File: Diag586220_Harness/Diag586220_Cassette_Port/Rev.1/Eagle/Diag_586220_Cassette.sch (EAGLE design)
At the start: 11 parts, among them J1 C64-TAPEPORT, J4 C64-TAPEPORTM, Q1 BC547B

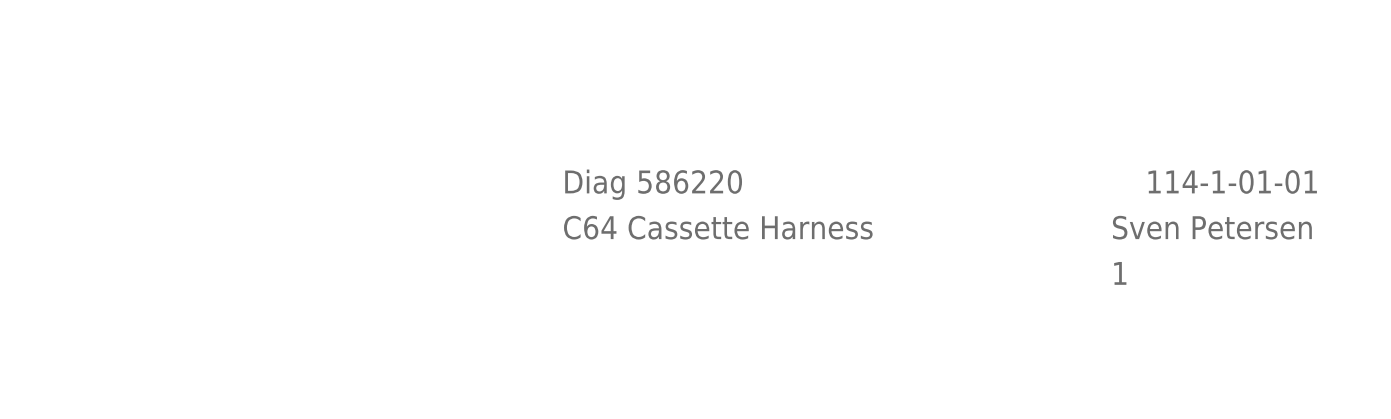
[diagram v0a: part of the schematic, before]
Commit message: Silk SCreen Update
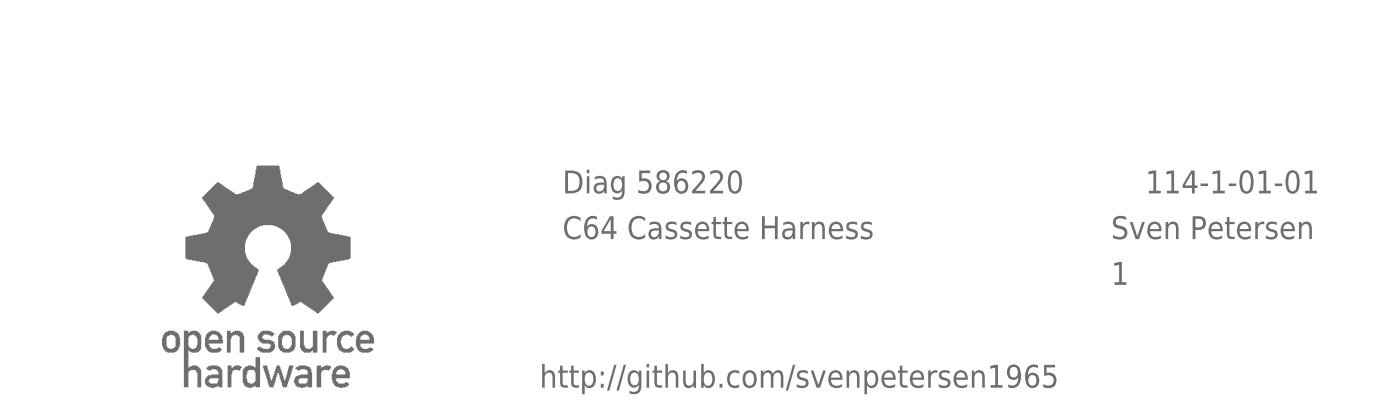
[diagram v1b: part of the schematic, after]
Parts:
- added U$18: OPEN_SOURCE_HW, Logo:OPEN_SOURCE_HW
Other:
- note added: "http://github.com/svenpetersen1965"
